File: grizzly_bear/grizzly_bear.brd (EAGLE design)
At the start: 71.1 x 39.4 mm, 58 parts, among them Q1 N-CHANNEL-MOSFET, Q2 N-CHANNEL-MOSFET, Q3 N-CHANNEL-MOSFET, Q4 N-CHANNEL-MOSFET, Q5 IPD90P03P4L, U1 A4940, U2 ATMEGA32U4-AU, U3 ACS714, U4 UA78L00, Y1 16MHz

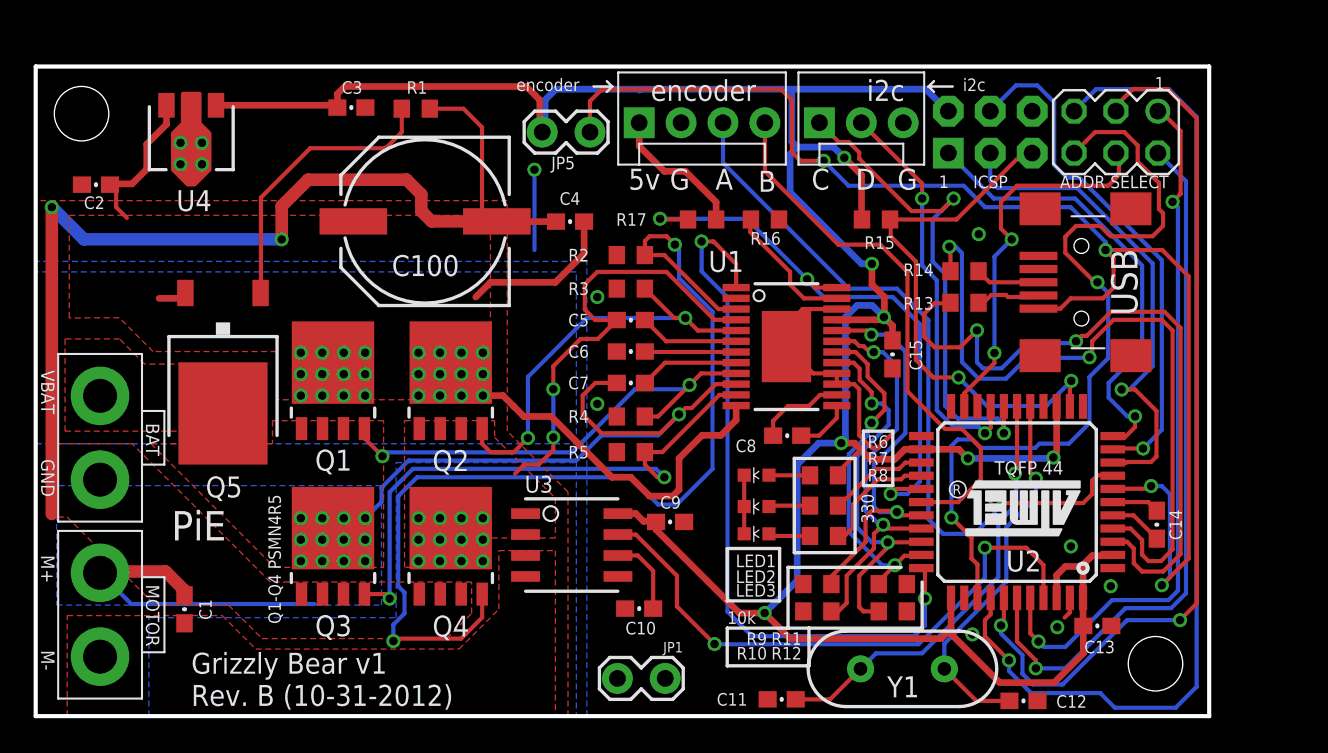
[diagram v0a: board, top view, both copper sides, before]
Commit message: Grizzly Bear rev C (mostly fixing crystal issues)
Change-Id: I264842dbfa1f0f907bc054e42f2a839b1c56a3fa
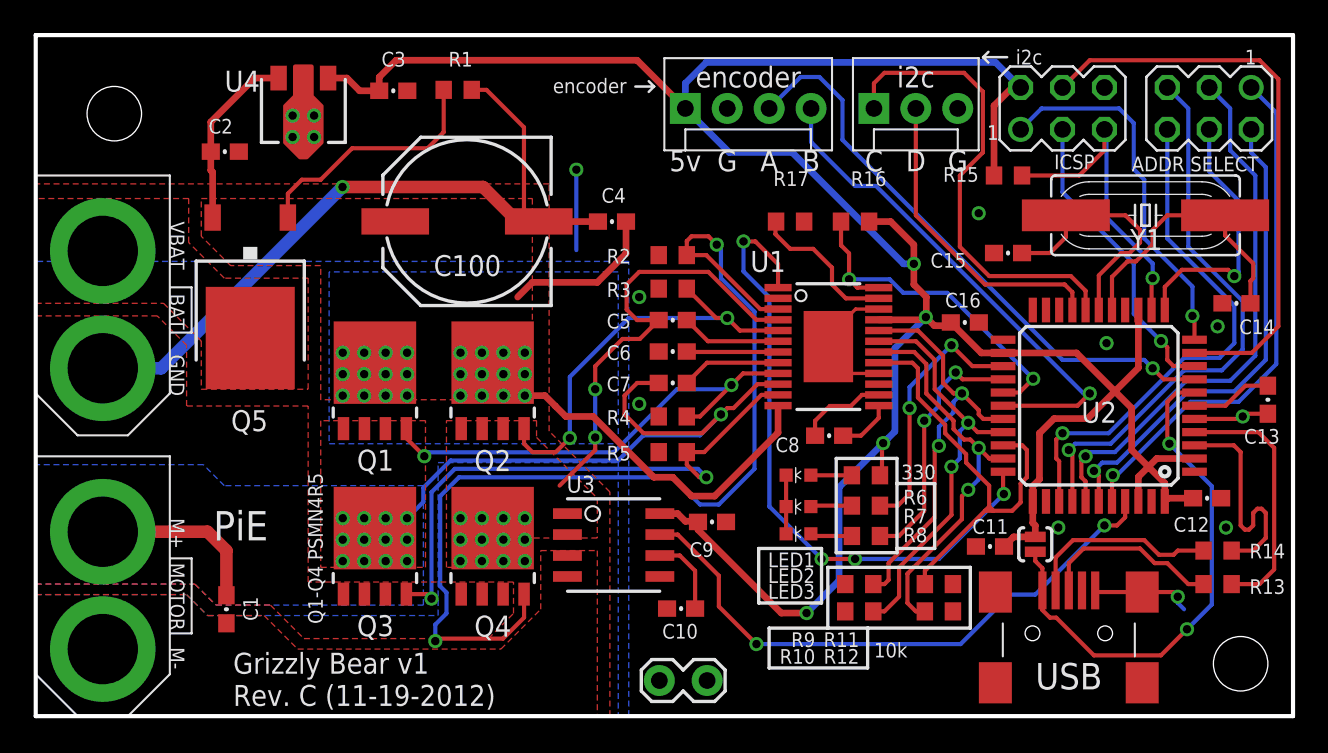
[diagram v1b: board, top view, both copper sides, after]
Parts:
- removed JP1.0, JP2.0: (no value), pie:1X02_XTRA_BIG
- removed JP5: (no value), pie:1X02_LOCK
- removed U$15, U$16: (no value), SparkFun-Electromechanical:STAND-OFF
- added C16: 0.1uF, pie:0603-CAP
- added SJ1: SOLDERJUMPERNO, pie:SJ_2S-NO
- added STANDOFF1, STANDOFF2: STAND-OFF, pie:STAND-OFF
- added U$18, U$19: XT60CONNECTOR, pie:XT60CONNECTOR
- C11, C12: value 18pF -> 0.1uF
- C14, C15: value 0.1uF -> 18pF
- JP6: value AVR_SPI_PRG_6NS -> AVR_SPI_PRG_6MA03-2; device pie:2X3-NS -> pie:MA03-2
- R16: value 47k -> 10k
- R17: value 10k -> 47k
- Y1: device pie:HC49US -> pie:HC49UP
- moved Y1 31.2 mm to (67.3, 30.4)
- moved R13 22.9 mm to (71.6, 8.00), turned to 0 degrees
- moved R14 22.8 mm to (71.6, 10.0), turned to 0 degrees
- moved U$2 18.8 mm to (62.6, 7.62), turned to 0 degrees
- moved C13 17.2 mm to (74.7, 19.2), turned to 270 degrees
- moved C12 16.6 mm to (71.0, 13.2), turned to 0 degrees
- moved C11 15.7 mm to (57.8, 10.3)
- moved C14 14.3 mm to (72.8, 25.0), turned to 0 degrees
- moved C15 9.32 mm to (58.9, 28.1), turned to 0 degrees
- moved R15 8.43 mm to (58.9, 32.8)
- moved C2 8.06 mm to (11.5, 34.2), turned to 0 degrees
- moved U2 7.66 mm to (64.4, 18.8)
- moved U4 6.99 mm to (16.2, 34.8)
- moved SV1 5.83 mm to (71.1, 36.8)
- moved R16 5.46 mm to (49.7, 30.0)
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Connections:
- net 5V: now also C11.2, C12.1, C16.1, R16.2, SJ1.1; no longer C13.2, C15.1, JP5.1, R17.2
- net BATGND: now also U$18.GND; no longer JP1.0.1
- net DIP4: now also U2.12; no longer U2.21
- net FAULT: now also R16.1; no longer R17.1
- net GND: now also C12.2, C13.2, C14.1, C15.1, C16.2, R17.2; no longer C12.1, C13.1, C14.2, C15.2, R16.2
- net M+: now also U$19.12V; no longer JP2.0.2
- net M-(POST): now also U$19.GND; no longer JP2.0.1
- net N$18: now also C13.1; no longer C14.1
- net N$20: now also R11.1; no longer R12.1
- net N$21: now also R12.1; no longer R11.1
- net N$24: now also R13.1; no longer R14.1
- net N$26: now also C15.2; no longer C11.2
- net N$27: now also C14.2; no longer C12.2
- net N$29: now also R14.1; no longer R13.1
- net N$6: now also R17.1; no longer R16.1
- net N$7: now also R14.2; no longer R13.2
- net N$9: now also R13.2; no longer R14.2
- net VIN: now also U$18.12V; no longer JP1.0.2
- net VUSB: now also SJ1.2; no longer JP5.2
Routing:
- net VUSB: track 82.0 -> 31.7 mm, vias 4 -> 2
- net N$7: track 42.9 -> 14.0 mm, vias 2 -> 0
- net N$9: track 43.0 -> 15.5 mm, vias 2 -> 0
- net DIP5: track 61.2 -> 34.0 mm
- net DIP3: track 53.8 -> 33.2 mm, vias 2 -> 1
- net BATGND: track 63.6 -> 45.7 mm, vias 2 -> 1
- net DIP6: track 49.1 -> 31.7 mm, vias 2 -> 1
- net FAULT: track 35.8 -> 21.5 mm, vias 3 -> 2
- net DIP2: track 43.1 -> 29.5 mm
- net RESET: track 32.2 -> 19.1 mm, vias 2 -> 1
- net SCK: track 30.5 -> 18.4 mm
- net 5V: track 177.7 -> 166.4 mm, vias 7 -> 4
- net DIP1: track 42.9 -> 31.7 mm, vias 2 -> 1
- net N$26: track 26.2 -> 15.4 mm, vias 1 -> 0
- net RED: track 6.24 -> 15.9 mm, vias 0 -> 2
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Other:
- board size 71.1 x 39.4 mm -> 76.2 x 41.3 mm
- board text added: "Rev. C (11-19-2012)"
- board text removed: "Rev. B (10-31-2012)"

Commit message: Name all nets in grizzly bear
Change-Id: If62fb746465388608cda9341d957dc1d3d35e733
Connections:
- net M-(POST) renamed M-
- net N$1 renamed RPP-GATE
- net N$10 renamed DRIVER-RESET
- net N$11 renamed GLB
- net N$13 renamed GHB
- net N$14 renamed CB
- net N$16 renamed CA
- net N$17 renamed VREG
- net N$18 renamed UCAP
- net N$19 renamed CP1
- net N$2 renamed GHA
- net N$20 renamed BLO
- net N$21 renamed BHI
- net N$22 renamed ALO
- net N$23 renamed RED-LED
- net N$24 renamed D+-_CON
- net N$25 renamed POWER-LED
- net N$26 renamed XTAL1
- net N$27 renamed XTAL2
- net N$28 renamed FILTER
- net N$29 renamed D-_CON
- net N$3 renamed CP2
- net N$5 renamed GREEN-LED
- net N$6 renamed RDEAD
- net N$7 renamed D-
- net N$8 renamed GLA
- net N$9 renamed D+
- net SGH renamed SB
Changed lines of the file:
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@@
 <?xml version="1.0" encoding="utf-8"?>
 <!DOCTYPE eagle SYSTEM "eagle.dtd">
-<eagle version="6.2">
+<eagle version="6.3">
 <drawing>
 <settings>
@@
 </class>
 </classes>
-<designrules>
+<designrules name="advancedcircuits-33each-pie">
 <description language="de">&lt;b&gt;EAGLE Design Rules&lt;/b&gt;
 &lt;p&gt;
@@
 </elements>
 <signals>
-<signal name="N$2">
+<signal name="GHA">
 <contactref element="U1" pad="9"/>
 <contactref element="R4" pad="1"/>
@@
 <wire x1="30.86" y1="19.425" x2="31.4925" y2="18.7925" width="0.4064" layer="1"/>
 </signal>
-<signal name="N$8">
+<signal name="GLA">
 <contactref element="U1" pad="11"/>
 <contactref element="R5" pad="1"/>
@@
 <contactref element="Q3" pad="4"/>
 </signal>
-<signal name="N$11">
+<signal name="GLB">
 <contactref element="U1" pad="3"/>
 <contactref element="R2" pad="1"/>
@@
 <contactref element="Q4" pad="4"/>
 </signal>
-<signal name="N$13">
+<signal name="GHB">
 <contactref element="U1" pad="5"/>
 <contactref element="R3" pad="1"/>
@@
 <contactref element="Q2" pad="4"/>
 </signal>
-<signal name="N$14">
+<signal name="CB">
 <contactref element="C5" pad="2"/>
 <contactref element="U1" pad="6"/>
@@
 <wire x1="48.26" y1="22.175" x2="48.04" y2="22.395" width="0.2032" layer="1"/>
 </signal>
-<signal name="N$6">
+<signal name="RDEAD">
 <contactref element="R17" pad="1"/>
 <contactref element="U1" pad="23"/>
@@
 <wire x1="59.617" y1="19.612" x2="60.452" y2="20.447" width="0.254" layer="1"/>
 </signal>
-<signal name="N$19">
+<signal name="CP1">
 <contactref element="C8" pad="1"/>
 <contactref element="U1" pad="14"/>
@@
 <wire x1="50.077" y1="19.47" x2="49.403" y2="18.796" width="0.254" layer="1"/>
 </signal>
-<signal name="N$20">
+<signal name="BLO">
 <contactref element="U1" pad="17"/>
 <contactref element="R11" pad="1"/>
@@
 <wire x1="60.071" y1="16.129" x2="60.071" y2="14.478" width="0.254" layer="1"/>
 </signal>
-<signal name="N$21">
+<signal name="BHI">
 <contactref element="U1" pad="18"/>
 <contactref element="R12" pad="1"/>
@@
 <wire x1="57.15" y1="14.351" x2="57.15" y2="16.256" width="0.254" layer="16"/>
 </signal>
-<signal name="N$22">
+<signal name="ALO">
 <contactref element="U1" pad="19"/>
 <contactref element="R10" pad="1"/>
@@
 <wire x1="20.819" y1="38.726" x2="21.844" y2="39.751" width="0.4064" layer="1"/>
 </signal>
-<signal name="N$3">
+<signal name="CP2">
 <contactref element="C8" pad="2"/>
 <contactref element="U1" pad="13"/>
@@
 <wire x1="51.09" y1="18.82" x2="51.09" y2="18.07" width="0.254" layer="1"/>
 </signal>
-<signal name="N$17">
+<signal name="VREG">
 <contactref element="C6" pad="1"/>
 <contactref element="U1" pad="7"/>
@@
 <wire x1="7.604" y1="21.082" x2="18.592" y2="32.07" width="0.762" layer="16"/>
 </signal>
-<signal name="N$5">
+<signal name="GREEN-LED">
 <contactref element="R8" pad="2"/>
 <contactref element="LED3" pad="A"/>
@@
 <wire x1="47.108" y1="10.919" x2="46.978" y2="11.049" width="0.254" layer="1"/>
 </signal>
-<signal name="N$23">
+<signal name="RED-LED">
 <contactref element="LED2" pad="A"/>
 <contactref element="R7" pad="2"/>
@@
 <wire x1="47.035" y1="12.757" x2="46.978" y2="12.7" width="0.254" layer="1"/>
 </signal>
-<signal name="N$25">
+<signal name="POWER-LED">
 <contactref element="R6" pad="1"/>
 <contactref element="LED1" pad="A"/>
@@
 <wire x1="46.988" y1="14.595" x2="46.978" y2="14.605" width="0.254" layer="1"/>
 </signal>
-<signal name="N$28">
+<signal name="FILTER">
 <contactref element="U3" pad="6"/>
 <contactref element="C10" pad="2"/>
@@
 <wire x1="39.033" y1="9.735" x2="39.963" y2="8.805" width="0.254" layer="1"/>
 </signal>
-<signal name="N$26">
+<signal name="XTAL1">
 <contactref element="C15" pad="2"/>
 <contactref element="U2" pad="17"/>
@@
 <wire x1="59.778" y1="28.067" x2="61.468" y2="28.067" width="0.254" layer="1"/>
 </signal>
-<signal name="N$27">
+<signal name="XTAL2">
 <contactref element="C14" pad="2"/>
 <contactref element="U2" pad="16"/>
@@
 <wire x1="72.0852" y1="29.1338" x2="73.787" y2="27.432" width="0.254" layer="1"/>
 </signal>
-<signal name="N$16">
+<signal name="CA">
 <contactref element="C7" pad="1"/>
 <contactref element="U1" pad="8"/>
@@
 <wire x1="52.959" y1="18.669" x2="52.959" y2="13.462" width="0.254" layer="1"/>
 </signal>
-<signal name="N$1">
+<signal name="RPP-GATE">
 <contactref element="R1" pad="2"/>
 <wire x1="17.272" y1="32.512" x2="19.177" y2="34.417" width="0.254" layer="1"/>
@@
 <wire x1="16.129" y1="32.512" x2="17.272" y2="32.512" width="0.254" layer="1"/>
 </signal>
-<signal name="N$7">
+<signal name="D-">
 <contactref element="R14" pad="2"/>
 <contactref element="U2" pad="3"/>
@@
 <wire x1="73.025" y1="11.557" x2="73.025" y2="16.002" width="0.254" layer="1"/>
 </signal>
-<signal name="N$9">
+<signal name="D+">
 <contactref element="R13" pad="2"/>
 <contactref element="U2" pad="4"/>
@@
 <wire x1="75.057" y1="16.256" x2="74.101" y2="17.212" width="0.254" layer="1"/>
 </signal>
-<signal name="N$18">
+<signal name="UCAP">
 <contactref element="C13" pad="1"/>
 <contactref element="U2" pad="6"/>
@@
 <wire x1="73.318" y1="20.027" x2="72.103" y2="18.812" width="0.254" layer="1"/>
 </signal>
-<signal name="N$24">
+<signal name="D+-_CON">
 <contactref element="U$2" pad="D+"/>
 <contactref element="R13" pad="1"/>
@@
 <wire x1="69.85" y1="8.001" x2="70.778" y2="8.001" width="0.254" layer="1"/>
 </signal>
-<signal name="N$29">
+<signal name="D-_CON">
 <contactref element="U$2" pad="D-"/>
 <contactref element="R14" pad="1"/>
@@
 <wire x1="71.277503125" y1="6.769" x2="69.774003125" y2="5.2655" width="0.254" layer="16"/>
 </signal>
-<signal name="N$4">
-</signal>
-<signal name="N$10">
+<signal name="DRIVER-RESET">
 <contactref element="U2" pad="33"/>
 <contactref element="U1" pad="1"/>
@@
 <wire x1="54.737" y1="9.525" x2="58.674" y2="13.462" width="0.254" layer="16"/>
 </signal>
-<signal name="SGH">
+<signal name="SB">
 <contactref element="C5" pad="1"/>
 <contactref element="U1" pad="4"/>
@@
 <wire x1="33.909" y1="16.129" x2="31.75" y2="13.97" width="0.254" layer="1"/>
 </signal>
-<signal name="M-(POST)">
+<signal name="M-">
 <contactref element="U3" pad="4"/>
 <contactref element="U3" pad="3"/>

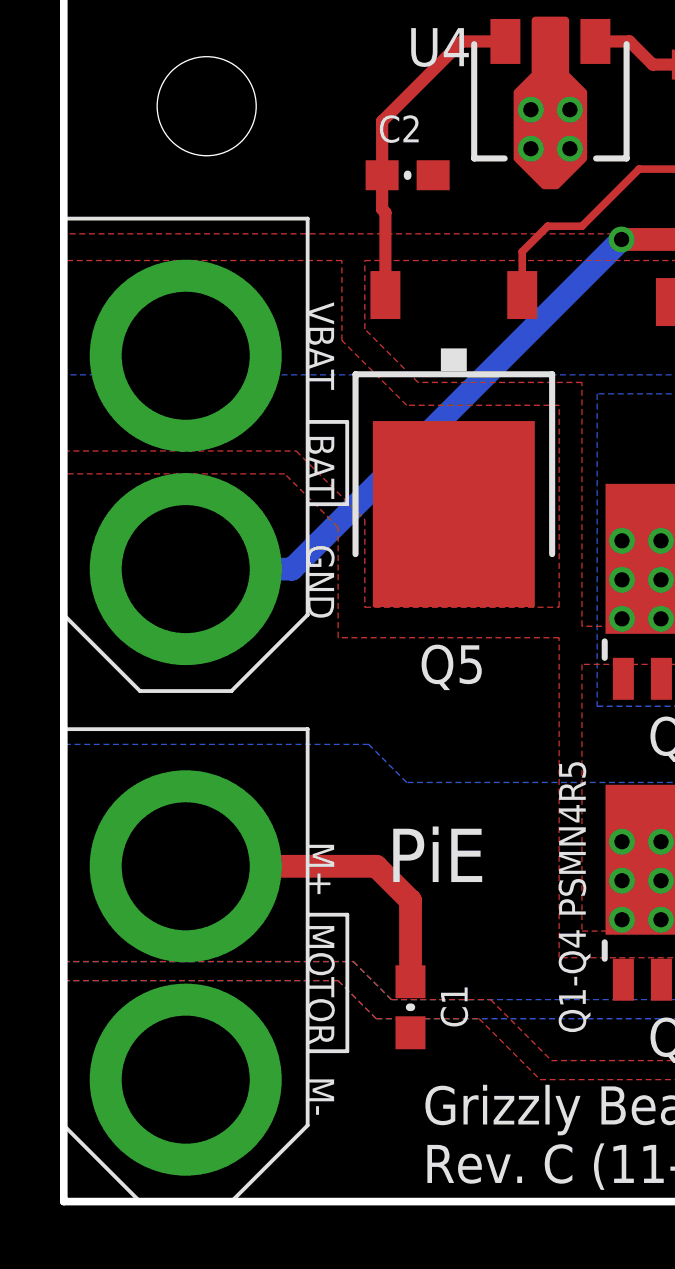
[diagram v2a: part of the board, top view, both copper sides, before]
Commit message: Fixed XT60 connector in pie.lbr. Changed battery connector on sherlock to have 4 pins instead of 5. Replaced XT60 on sherlock, solenoid board, and grizzly bear with new version.
Change-Id: Ic4b688068eb477e37db8d2c4f2efb7678e25c5b6
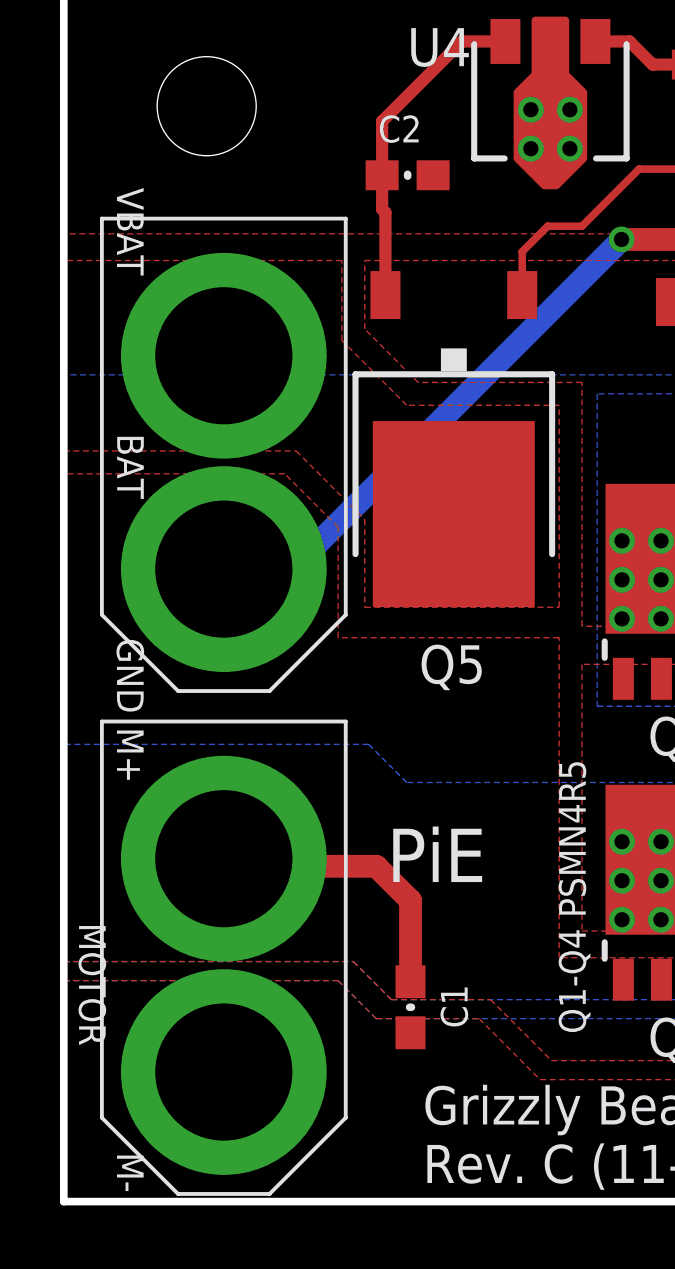
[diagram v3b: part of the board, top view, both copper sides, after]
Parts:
- moved U$19 1.30 mm to (1.27, 16.0)
- moved U$18 1.27 mm to (1.27, 32.8)
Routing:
- net BATGND: track 45.7 -> 44.5 mm
- net M+: track 47.6 -> 46.6 mm
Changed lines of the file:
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@@
 <text x="43.18" y="39.37" size="1.27" layer="21" font="vector" ratio="15" align="top-center">encoder</text>
 <text x="60.198" y="40.386" size="0.889" layer="21" font="vector" ratio="20" align="top-center">i2c</text>
-<text x="9.0115" y="20.6555" size="0.889" layer="21" font="vector" ratio="15" rot="SR270" align="top-center">GND</text>
-<text x="9.0115" y="28.5225" size="0.889" layer="21" font="vector" ratio="15" rot="SR270" align="top-center">VBAT</text>
-<text x="9.0115" y="11.0665" size="0.889" layer="21" font="vector" ratio="15" rot="SR270" align="top-center">M+</text>
-<text x="9.0115" y="3.5095" size="0.889" layer="21" font="vector" ratio="15" rot="SR270" align="top-center">M-</text>
-<text x="9.017" y="24.511" size="0.889" layer="21" font="vector" ratio="15" rot="SR270" align="top-center">BAT</text>
-<text x="9.017" y="7.239" size="0.889" layer="21" font="vector" ratio="15" rot="SR270" align="top-center">MOTOR</text>
-<wire x1="8.151" y1="9.563" x2="9.451" y2="9.563" width="0.127" layer="21"/>
-<wire x1="9.451" y1="9.563" x2="9.451" y2="5.013" width="0.127" layer="21"/>
-<wire x1="9.451" y1="5.013" x2="8.151" y2="5.013" width="0.127" layer="21"/>
-<wire x1="8.151" y1="25.988" x2="9.447" y2="25.988" width="0.127" layer="21"/>
-<wire x1="9.447" y1="25.988" x2="9.447" y2="23.246" width="0.127" layer="21"/>
-<wire x1="9.447" y1="23.246" x2="8.151" y2="23.246" width="0.127" layer="21"/>
+<text x="2.6615" y="17.526" size="0.889" layer="21" font="vector" ratio="15" rot="SR270" align="top-center">GND</text>
+<text x="2.6615" y="32.3325" size="0.889" layer="21" font="vector" ratio="15" rot="SR270" align="top-center">VBAT</text>
+<text x="2.6615" y="14.8765" size="0.889" layer="21" font="vector" ratio="15" rot="SR270" align="top-center">M+</text>
+<text x="2.6615" y="0.9695" size="0.889" layer="21" font="vector" ratio="15" rot="SR270" align="top-center">M-</text>
+<text x="2.667" y="24.511" size="0.889" layer="21" font="vector" ratio="15" rot="SR270" align="top-center">BAT</text>
+<text x="1.397" y="7.239" size="0.889" layer="21" font="vector" ratio="15" rot="SR270" align="top-center">MOTOR</text>
 <text x="11.965" y="0.62" size="1.27" layer="21" font="vector" ratio="15">Rev. C (11-19-2012)</text>
 <text x="11.965" y="2.57" size="1.27" layer="21" font="vector" ratio="15">Grizzly Bear v1</text>
@@
 <attribute name="VALUE" x="66.294" y="10.16" size="0.889" layer="27" font="vector" ratio="20"/>
 </element>
-<element name="U$18" library="pie" package="XT60CONNECTOR" value="XT60CONNECTOR" x="0" y="32.766" rot="R270"/>
-<element name="U$19" library="pie" package="XT60CONNECTOR" value="XT60CONNECTOR" x="0" y="15.748" rot="R270"/>
+<element name="U$18" library="pie" package="XT60CONNECTOR" value="XT60CONNECTOR" x="1.27" y="32.766" rot="R270"/>
+<element name="U$19" library="pie" package="XT60CONNECTOR" value="XT60CONNECTOR" x="1.27" y="16.002" rot="R270"/>
 <element name="STANDOFF1" library="pie" package="STAND-OFF" value="STAND-OFF" x="4.7625" y="36.5125"/>
 <element name="STANDOFF2" library="pie" package="STAND-OFF" value="STAND-OFF" x="73.025" y="3.175"/>
@@
 <contactref element="Q3" pad="MB"/>
 <contactref element="U$19" pad="12V"/>
-<wire x1="4.064" y1="11.176" x2="10.414" y2="11.176" width="0.762" layer="1"/>
 <wire x1="10.414" y1="11.176" x2="11.557" y2="10.033" width="0.762" layer="1"/>
 <wire x1="11.557" y1="7.327" x2="11.557" y2="10.033" width="0.762" layer="1"/>
+<wire x1="10.414" y1="11.176" x2="5.334" y2="11.176" width="0.762" layer="1"/>
+<wire x1="5.334" y1="11.176" x2="5.334" y2="11.43" width="0.4064" layer="1"/>
 </signal>
 <signal name="ISENSE">
@@
 <contactref element="Q4" pad="1"/>
 <contactref element="U$18" pad="GND"/>
-<wire x1="4.064" y1="21.082" x2="7.604" y2="21.082" width="0.762" layer="16"/>
+<wire x1="5.334" y1="21.082" x2="7.604" y2="21.082" width="0.762" layer="16"/>
 <wire x1="18.592" y1="32.07" x2="27.112" y2="32.07" width="0.762" layer="1"/>
 <wire x1="26.425" y1="37.956" x2="27.322" y2="37.956" width="0.254" layer="1"/>
